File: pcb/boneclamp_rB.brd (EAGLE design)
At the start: 160 x 100 mm, 63 parts, among them IC1 24C, U1 AD7656YSTZ, U2 LT1964ES5-5TRMPBF, U3 LT1962EMS8-5PBF, U7 AD7682BCPZ, U8 TPS63700DRCT

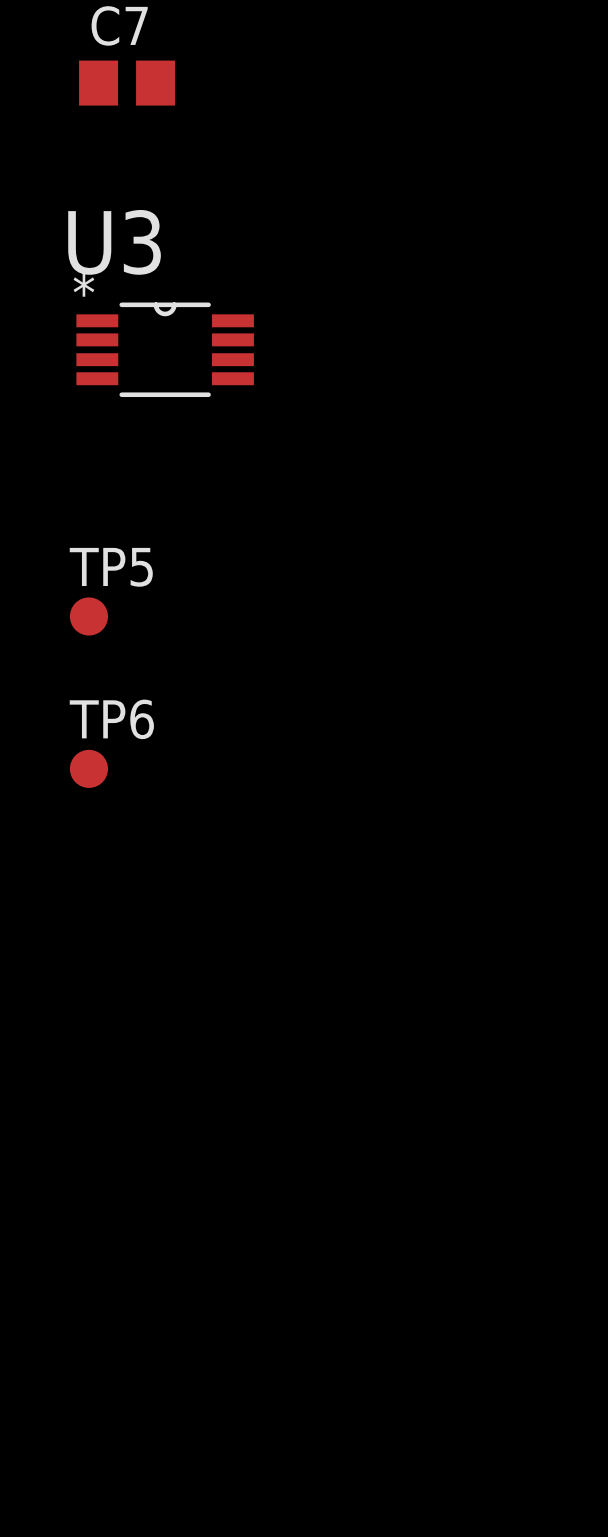
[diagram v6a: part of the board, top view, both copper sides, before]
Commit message: Finished power supply circuits on schematic. Updated BOM and added new data sheets.
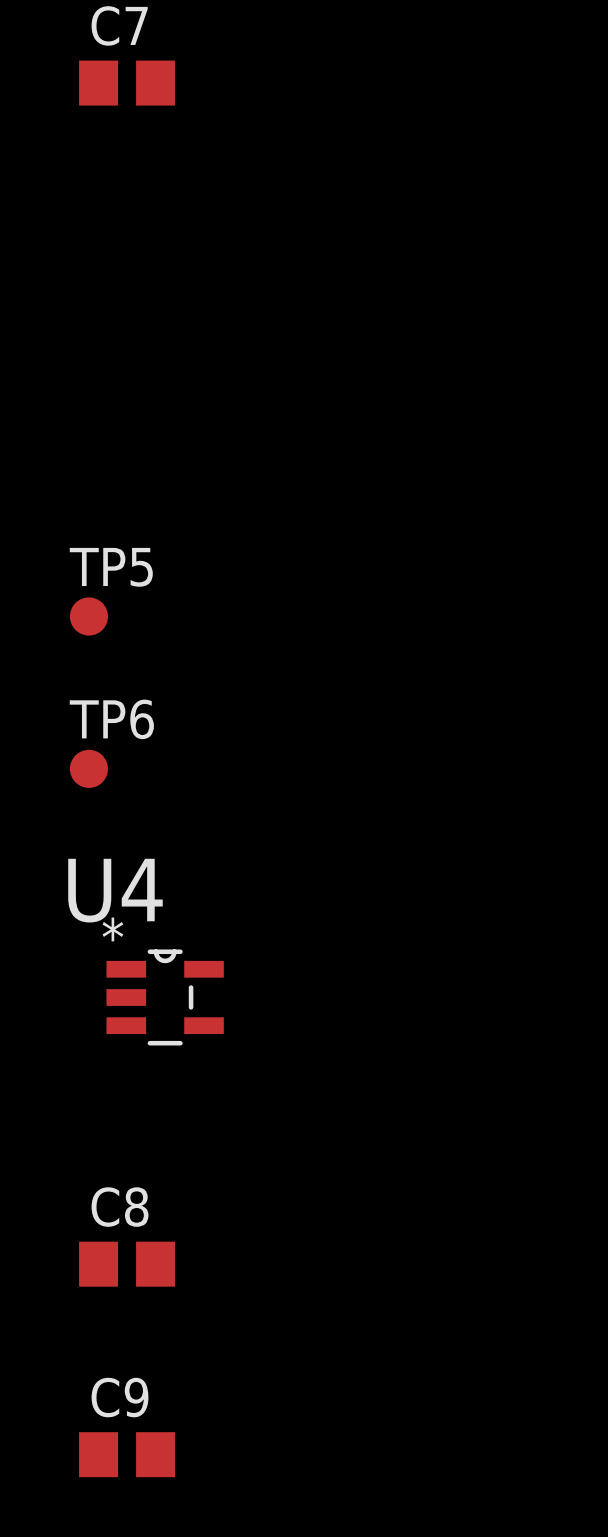
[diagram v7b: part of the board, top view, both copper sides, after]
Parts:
- removed U3: LT1962EMS8-5PBF, linear-extended-01:SOP65P490X110-8N
- added C8, C9: 1uF, rcl:C0805
- added U4: TLV70245DBVT, ti-extended:SOT95P280X110-5N
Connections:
- removed net IN: U3.8
- net AGND: now also C8.2, C9.2, U4.2
- net VDD: now also C9.1, U4.5
- net VDD_5V: now also C8.1, U4.1, U4.3
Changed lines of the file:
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@@
 <element name="C6" library="rcl" package="C0805" value="10nF" x="-83.82" y="-184.15"/>
 <element name="C7" library="rcl" package="C0805" value="10uF" x="-83.82" y="-190.5"/>
-<element name="U3" library="linear-extended-01" package="SOP65P490X110-8N" value="LT1962EMS8-5PBF" x="-82.55" y="-199.39">
-<attribute name="PACKAGE" value="MSOP-8" x="-82.55" y="-199.39" size="1.778" layer="27" display="off"/>
-<attribute name="OC_NEWARK" value="57M7401" x="-82.55" y="-199.39" size="1.778" layer="27" display="off"/>
-<attribute name="MPN" value="LT1962EMS8-5#PBF" x="-82.55" y="-199.39" size="1.778" layer="27" display="off"/>
-<attribute name="SUPPLIER" value="Linear Technologies" x="-82.55" y="-199.39" size="1.778" layer="27" display="off"/>
-<attribute name="OC_FARNELL" value="1273624" x="-82.55" y="-199.39" size="1.778" layer="27" display="off"/>
-</element>
 <element name="TP5" library="testpad" package="B1,27" value="TPB1,27" x="-85.09" y="-208.28">
 <attribute name="TP_SIGNAL_NAME" value="" x="-85.09" y="-208.28" size="1.778" layer="27" display="off"/>
@@
 <attribute name="TP_SIGNAL_NAME" value="" x="-85.09" y="-213.36" size="1.778" layer="27" display="off"/>
 </element>
+<element name="U4" library="ti-extended" package="SOT95P280X110-5N" value="TLV70245DBVT" x="-82.55" y="-220.98">
+<attribute name="PACKAGE" value="TSOT-23-5" x="-82.55" y="-220.98" size="1.778" layer="27" display="off"/>
+<attribute name="OC_NEWARK" value="64R0678" x="-82.55" y="-220.98" size="1.778" layer="27" display="off"/>
+<attribute name="MPN" value="TLV70025DDCR" x="-82.55" y="-220.98" size="1.778" layer="27" display="off"/>
+<attribute name="SUPPLIER" value="Texas Instruments" x="-82.55" y="-220.98" size="1.778" layer="27" display="off"/>
+<attribute name="OC_FARNELL" value="-" x="-82.55" y="-220.98" size="1.778" layer="27" display="off"/>
+</element>
+<element name="C8" library="rcl" package="C0805" value="1uF" x="-83.82" y="-229.87"/>
+<element name="C9" library="rcl" package="C0805" value="1uF" x="-83.82" y="-236.22"/>
 </elements>
 <signals>
@@
 <contactref element="U7" pad="20"/>
 <contactref element="U$42" pad="5"/>
+<contactref element="U4" pad="5"/>
+<contactref element="C9" pad="1"/>
 <wire x1="-71.3994" y1="-20.6502" x2="99.695" y2="95.9612" width="0" layer="19" extent="1-1"/>
 <wire x1="-83.5406" y1="-18.542" x2="-71.3994" y2="-20.6502" width="0" layer="19" extent="1-1"/>
+<wire x1="-81.2546" y1="-220.0402" x2="-71.3994" y2="-20.6502" width="0" layer="19" extent="1-1"/>
+<wire x1="-84.77" y1="-236.22" x2="-81.2546" y2="-220.0402" width="0" layer="19" extent="1-1"/>
 </signal>
 <signal name="DVCC">
@@
 <contactref element="C6" pad="2"/>
 <contactref element="C7" pad="2"/>
+<contactref element="C9" pad="2"/>
+<contactref element="C8" pad="2"/>
+<contactref element="U4" pad="2"/>
 <wire x1="-82.87" y1="-177.8" x2="-83.7692" y2="-167.9702" width="0" layer="19" extent="1-1"/>
 <wire x1="-82.87" y1="-184.15" x2="-82.87" y2="-177.8" width="0" layer="19" extent="1-1"/>
@@
 <wire x1="-82.55" y1="-60.96" x2="-81.0768" y2="-61.468" width="0" layer="19" extent="1-1"/>
 <wire x1="-84.0232" y1="-60.452" x2="-82.55" y2="-60.96" width="0" layer="19" extent="1-1"/>
+<wire x1="-83.8454" y1="-220.98" x2="-82.87" y2="-190.5" width="0" layer="19" extent="1-1"/>
+<wire x1="-82.87" y1="-229.87" x2="-83.8454" y2="-220.98" width="0" layer="19" extent="1-1"/>
+<wire x1="-82.87" y1="-236.22" x2="-82.87" y2="-229.87" width="0" layer="19" extent="1-1"/>
 <wire x1="1.905" y1="19.05" x2="-81.0768" y2="-61.468" width="0" layer="19" extent="1-1"/>
 <wire x1="4.445" y1="19.05" x2="1.905" y2="19.05" width="0" layer="19" extent="1-1"/>
@@
 <contactref element="C24" pad="1"/>
 <contactref element="R5" pad="1"/>
+<contactref element="U4" pad="1"/>
+<contactref element="C8" pad="1"/>
+<contactref element="U4" pad="3"/>
 <wire x1="-84.67" y1="-73.66" x2="-84.77" y2="-78.74" width="0" layer="19" extent="1-1"/>
 <wire x1="-84.77" y1="-69.85" x2="-84.67" y2="-73.66" width="0" layer="19" extent="1-1"/>
 <wire x1="-84.0232" y1="-61.9506" x2="-84.77" y2="-69.85" width="0" layer="19" extent="1-1"/>
+<wire x1="-83.8454" y1="-220.0402" x2="-84.77" y2="-78.74" width="0" layer="19" extent="1-1"/>
+<wire x1="-83.8454" y1="-221.9198" x2="-83.8454" y2="-220.0402" width="0" layer="19" extent="1-1"/>
+<wire x1="-84.77" y1="-229.87" x2="-83.8454" y2="-221.9198" width="0" layer="19" extent="1-1"/>
 <wire x1="50.165" y1="24.13" x2="-84.0232" y2="-61.9506" width="0" layer="19" extent="1-1"/>
 <wire x1="52.705" y1="24.13" x2="50.165" y2="24.13" width="0" layer="19" extent="1-1"/>
@@
 <wire x1="-84.77" y1="-184.15" x2="-83.7692" y2="-169.8498" width="0" layer="19" extent="1-1"/>
 </signal>
-<signal name="IN">
-<contactref element="U3" pad="8"/>
-</signal>
 </signals>

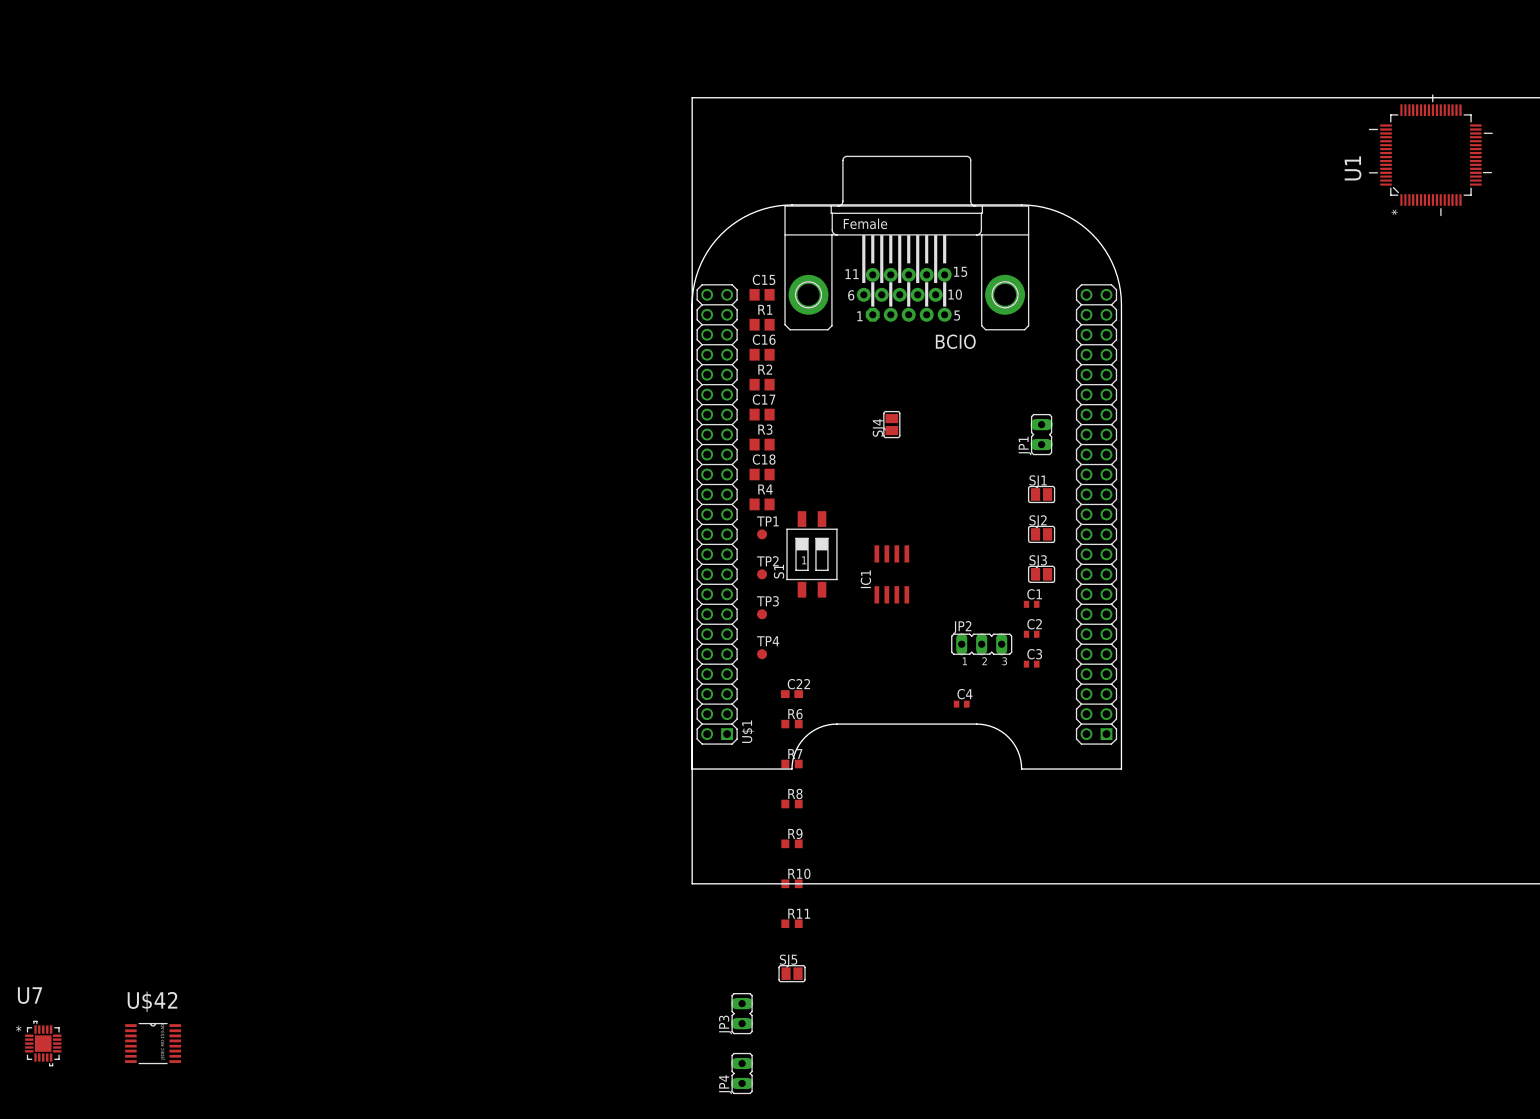
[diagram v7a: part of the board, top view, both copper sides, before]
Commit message: Updated adafruit library with 2X5 0.1 inch pitch header, which we will use for I/O on the BC. Added that to the schematic
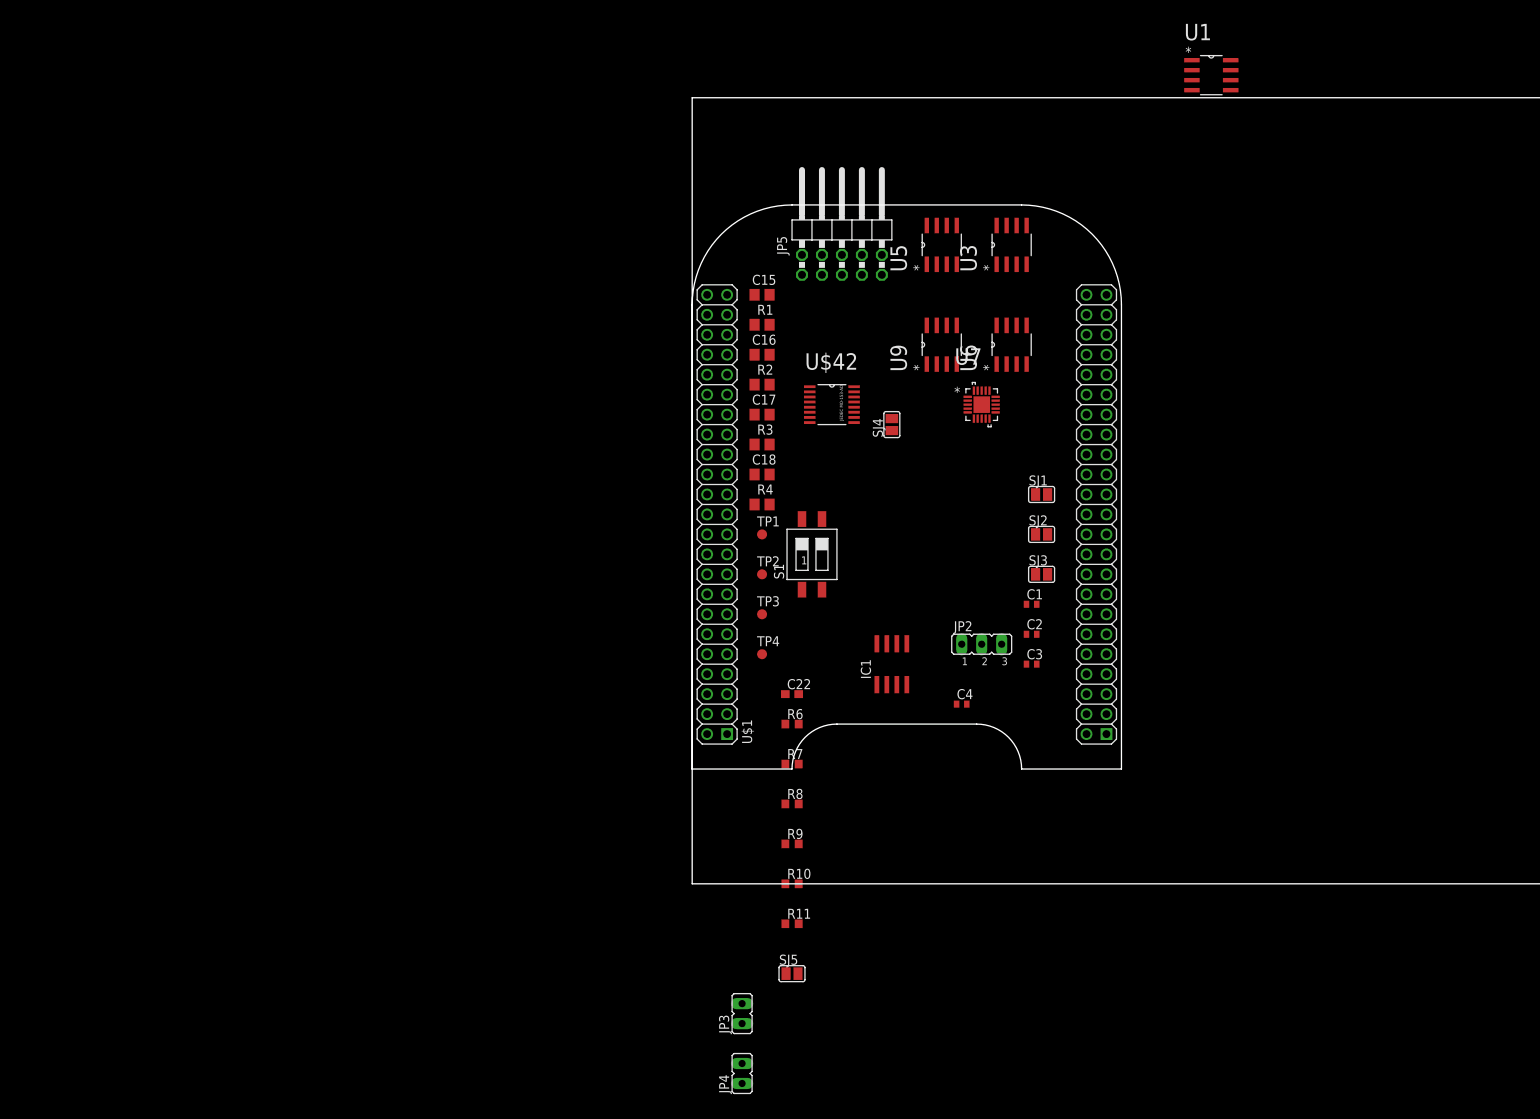
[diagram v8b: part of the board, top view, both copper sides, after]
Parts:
- removed BCIO: F15-SHEILD, adafruit:HDF15H
- removed JP1: (no value), jumper:JP1
- added JP5: PINHD-2X5/90, adafruit:2X05/90
- added U3, U5, U6, U9: ADA4841-2YRZ, analog-devices-01:SOIC127P600X175-8N
- U1: value AD7656YSTZ -> ADA4841-2YRZ; device analog-devices-01:QFP50P1200X1200X160-64N -> analog-devices-01:SOIC127P600X175-8N
- moved U7 144.4 mm to (36.8, 61.0)
- moved U$42 118.6 mm to (17.8, 61.0)
- moved U1 29.7 mm to (66.0, 102.9), turned to 0 degrees
- moved IC1 11.4 mm to (25.4, 27.9)
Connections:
- removed net CONVST: U1.21, U1.22, U1.23
- removed net DVCC: U1.26
- new net +VS: U1.8, U6.8, U9.8
- new net -VS: U1.4, U6.4, U9.4
- new net ADC_A: JP5.4
- new net ADC_B: JP5.6
- new net ADC_C: JP5.8
- new net ADC_D: JP5.10
- new net N$15: U3.1, U5.1
- new net N$26: U3.7, U5.7
- net AGND: no longer BCIO.1, JP1.2, U1.32, U1.37, U1.38, U1.43, U1.44, U1.49, U1.52, U1.53, U1.57, U1.59
- net DAC_A: now also JP5.3; no longer BCIO.8
- net DAC_B: now also JP5.5; no longer BCIO.9
- net DAC_C: now also JP5.7; no longer BCIO.10
- net DAC_D: now also JP5.9; no longer BCIO.11
- net DGND: no longer U1.25, U1.8
- net N$1: now also U3.8, U5.8; no longer BCIO.2, U1.33
- net N$10: no longer U1.56
- net N$11: no longer U1.58
- net N$12: no longer U1.27
- net N$13: no longer U1.34, U1.35, U1.40, U1.41, U1.46, U1.47, U1.50, U1.60
- net N$2: now also U3.3, U5.3; no longer BCIO.3, U1.36
- net N$20: no longer U1.51
- net N$3: now also U3.2, U5.2; no longer BCIO.4, U1.39
- net N$4: now also U3.5, U5.5; no longer BCIO.5, U1.42
- net N$5: now also U3.6, U5.6; no longer BCIO.6, U1.45
- net N$6: now also U3.4, U5.4; no longer BCIO.7, U1.48
- net SGND: now also JP5.1, JP5.2; no longer BCIO.P$1, BCIO.P$2, JP1.1
- net VDD: no longer U1.31
- net VSS: no longer U1.30
